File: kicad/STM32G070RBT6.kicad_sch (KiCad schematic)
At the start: 13 parts, among them J21 STM32-PROGRAM, J23 STM32-PROGRAM, U17 STM32G070RBT6, Y3 CRY-8MHz-3225-SMD

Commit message: Added Pi CM4/CM5
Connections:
- net CURENT-SENSE is gone; now on net PWR-BTN-SENSE: U17.17 (PA0)
- net VBAT-SENSE is gone; now on net PMIC_PWRON: U17.18 (PA1)
- net PMIC_PWRON: no longer U17.44 (PA12)
- net PWR-BTN-SENSE: no longer U17.43 (PA11)
- net CHARGE-STATUS renamed ~{CHG_INT}
- net MAIN-FAN-S-CTRL renamed SUCTION-FAN-FG
- net MAIN-FAN-S-SENSE renamed SUCTION-FAN-SP
- net RK-RESET renamed PI-RESET
- net V-CHARGE-SENSE renamed BAT_ID
- new net I2C2_SCL: U17.43 (PA11)
- new net I2C2_SDA: U17.44 (PA12)

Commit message: Changed MCU to STM32G473VCT6
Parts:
- removed C101: 100nF, oomwoo_altium:CAP-0402, symbol DesignLibrary:MCU-STM32_2_Capacitor-1_DesignLibrary.SchLib
- removed C102: 4.7uF, oomwoo_altium:CAP-0603, symbol DesignLibrary:MCU-STM32_2_Capacitor-1_DesignLibrary.SchLib
- removed C106, C107: 18pF, oomwoo_altium:CAP-0402, symbol DesignLibrary:MCU-STM32_2_Capacitor-1_DesignLibrary.SchLib
- removed C18: 100nF, oomwoo_altium:CAP-0402, symbol DesignLibrary:MCU-STM32_3_Capacitor-1_DesignLibrary.SchLib
- removed D15: SS34/NC, oomwoo_altium:SMA, symbol DesignLibrary:MCU-STM32_0_DIODE-2_DesignLibrary.SchLib
- removed J21: STM32-PROGRAM, oomwoo_altium:HDR1X5, symbol DesignLibrary:MCU-STM32_0_mirrored_HDRx5_DesignLibrary.SchLib
- removed R134: 10K, oomwoo_altium:RES-0402, symbol DesignLibrary:MCU-STM32_3_Resistor-1_DesignLibrary.SchLib
- removed R135: 0.01R, oomwoo_altium:RES-0805-S, symbol DesignLibrary:MCU-STM32_2_Resistor-1_DesignLibrary.SchLib
- removed R86: 0R, oomwoo_altium:RES-0402, symbol DesignLibrary:MCU-STM32_0_Resistor-1_DesignLibrary.SchLib
- removed U17: STM32G070RBT6, oomwoo_altium:QFP50P1200X1200X160-64N, symbol DesignLibrary:MCU-STM32_0_STM32G070RBT6_DesignLibrary.SchLib
- removed Y3: CRY-8MHz-3225-SMD, oomwoo_altium:X4B250_320H120_SMD, symbol DesignLibrary:MCU-STM32_0_CRY-24MHz-3225-SMD_0_DesignLibrary.SchLib
- added C12, C13, C14, C15, C16, C30, C32, C37: 100nF/10V, Capacitor_SMD:C_0603_1608Metric, symbol Device:C_Small
- added C17, C31, C33: 4.7uF/10V, Capacitor_SMD:C_0603_1608Metric, symbol Device:C_Small
- added C34, C35: 22pF/10V, Capacitor_SMD:C_0603_1608Metric, symbol Device:C_Small
- added D3, D5: SS34, Diode_SMD:D_SMA, symbol Diode:SS34
- added J21: STM-PROGRAM, Connector_PinHeader_2.54mm:PinHeader_1x05_P2.54mm_Vertical, symbol Connector:Conn_01x05_Pin
- added JTAG1: STLINK-V3MINIE, JLCImport:FTSH-107-01-L-DV-K-A, symbol JLCImport:FTSH-107-01-L-DV-K-A
- added R16: 0.01, Resistor_SMD:R_0603_1608Metric, symbol Device:R_US
- added R19: 0, Resistor_SMD:R_0603_1608Metric, symbol Device:R_US
- added R21, R22: 10k, Resistor_SMD:R_0603_1608Metric, symbol Device:R_US
- added R33: 10, Resistor_SMD:R_0603_1608Metric, symbol Device:R_US
- added U13: STM32G473VCT6, footprints:LQFP100-14x14mm, symbol 2026-07-20_14-00-45:STM32G473VCT6
- added X1: ABM3-8_000MHZ-D2Y-T, JLCImport:ABM3-8_000MHZ-D2Y-T, symbol JLCImport:ABM3-8_000MHZ-D2Y-T
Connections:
- net ANTI-FALL-LEFT-DOWN-ADC: now also U13.21 (PA1)
- net ANTI-FALL-LEFT-UP-ADC: now also U13.20 (PA0)
- net ANTI-FALL-RIGHT-DOWN-ADC: now also U13.25 (PA3)
- net ANTI-FALL-RIGHT-UP-ADC: now also U13.22 (PA2)
- net BAT_ID: now also U13.53 (PB14)
- net GND: now also C12.2, C13.2, C14.2, C15.2, C16.2, C17.2, C30.2, C31.2, C32.2, C33.2, C34.2, C35.2, C37.2, J21.4 (Pin_4), JTAG1.05 (5), JTAG1.07 (7), R22.1, U13.23 (VSS), U13.35 (VSSA), U13.48 (VSS), U13.63 (VSS), U13.74 (VSS), U13.99 (VSS)
- net HOME-BTN: now also U13.79 (PC10)
- net IMU-FSYNC: now also U13.86 (PD4)
- net IMU-INT#1: now also U13.85 (PD3)
- net IMU-INT#2: now also U13.84 (PD2)
- net IMU-SPI-CS: now also U13.93 (PB6)
- net IMU-SPI-MISO: now also U13.91 (PB4)
- net IMU-SPI-MOSI: now also U13.92 (PB5)
- net IMU-SPI-SCLK: now also R33.2
- net LED-HOME: now also U13.80 (PC11)
- net LED-PWR: now also U13.28 (PA6)
- net LiDAR-M-CTRL: now also U13.17 (PC2)
- net MAIN-FAN-V-CTRL: now also U13.82 (PD0)
- net PC14: now also U13.8 (PC14-OSC32_IN)
- net PC15: now also U13.9 (PC15-OSC32_OUT)
- net PI-RESET: now also U13.52 (PB13)
- net PMIC_PWRON: now also U13.73 (PA12)
- net PWR-BTN-SENSE: now also U13.72 (PA11)
- net SIDE-PROXI-LEFT: now also U13.87 (PD5)
- net SIDE-PROXI-RIGHT: now also U13.55 (PD8)
- net STM-PWR-CTRL: now also U13.78 (PA15)
- net STM-RESET: now also C37.1, J21.3 (Pin_3), JTAG1.12, R21.1, U13.14 (PG10-NRST)
- net STM32-SWCLK: now also J21.2 (Pin_2), JTAG1.06 (6), U13.77 (PA14)
- net STM32-SWDIO: now also J21.1 (Pin_1), JTAG1.04 (4), U13.76 (PA13)
- net STM32-UART1-RX: now also JTAG1.13, U13.31 (PC5)
- net STM32-UART1-TX: now also JTAG1.14, U13.30 (PC4)
- net TOUCHL: now also U13.88 (PD6)
- net TOUCHR: now also U13.56 (PD9)
- net VCC-3V3-P: now also C12.1, C13.1, C14.1, C15.1, C16.1, C17.1, C30.1, C31.1, C32.1, C33.1, D3.1 (K), D5.1 (K), R16.1, R21.2, U13.100 (VDD), U13.24 (VDD), U13.36 (VREF+), U13.37 (VDDA), U13.49 (VDD), U13.64 (VDD), U13.75 (VDD)
- net WATER-PUMP-SENSE-ADC: now also U13.27 (PA5)
- net WATER-PUMPU-CTRL: now also U13.15 (PC0)
- net WHEEL-M-L-F-ADC: now also U13.58 (PD11)
- net WHEEL-M-LEFT-ENCODE-A: now also U13.70 (PA9)
- net WHEEL-M-LEFT-IN1: now also U13.69 (PA8)
- net WHEEL-M-LEFT-IN2: now also U13.29 (PA7)
- net WHEEL-M-R-F-ADC: now also U13.57 (PD10)
- net WHEEL-M-RIGHT-ENCODE-A: now also U13.71 (PA10)
- net WHEEL-M-RIGHT-IN1: now also U13.94 (PB7)
- net WHEEL-M-RIGHT-IN2: now also U13.96 (PB9)
- net ~{CHG_INT}: now also U13.54 (PB15)
- new net: R19.1, U13.13 (PF1-OSC_OUT)
- new net: C35.1, R19.2, X1.2 (OSC2)
- new net: R33.1, U13.90 (PB3)
- new net: R22.2, U13.95 (PB8-BOOT0)
- new net: D5.2 (A), JTAG1.03 (3)
- new net: C34.1, U13.12 (PF0-OSC_IN), X1.1 (OSC1)
- new net: R16.2, U13.6 (VBAT)
- new net: D3.2 (A), J21.5 (Pin_5)
- new net I2C3_SCL: U13.67 (PC8)
- new net I2C3_SDA: U13.68 (PC9)
- new net MAIN-BRUSH-CURRENT-ADC: U13.26 (PA4)
- new net MAIN-BRUSH-IN1: U13.61 (PD14)
- new net MAIN-BRUSH-IN2: U13.62 (PD15)
- new net MAIN-FAN-S-CTRL: U13.83 (PD1)
- new net MAIN-FAN-S-SENSE: U13.81 (PC12)
- new net SIDE-BRUSH-CURRENT-ADC: U13.60 (PD13)
- new net SIDE-BRUSH-IN1: U13.65 (PC6)
- new net SIDE-BRUSH-IN2: U13.66 (PC7)
- no-connect marks 0 -> 36
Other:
- note added: "MCU STM32G473"
- note removed: "MCU STM32G070"
- moved on the sheet: J23

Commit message: STM32G473VCT6
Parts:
- removed D3: SS34, Diode_SMD:D_SMA, symbol Diode:SS34
- removed J21: STM-PROGRAM, Connector_PinHeader_2.54mm:PinHeader_1x05_P2.54mm_Vertical, symbol Connector:Conn_01x05_Pin
- removed J23: STM32-PROGRAM, oomwoo_altium:HDR1X5, symbol DesignLibrary:MCU-STM32_0_mirrored_HDRx5_DesignLibrary.SchLib
- removed R33: 10, Resistor_SMD:R_0603_1608Metric, symbol Device:R_US
- added MCU_IO1: Conn_02x24_Odd_Even, symbol Connector_Generic:Conn_02x24_Odd_Even
- added R64: 10, symbol Device:R_US
- added STM_DEBUG1: Conn_01x05_Pin, symbol Connector:Conn_01x05_Pin
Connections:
- net GND: now also MCU_IO1.10 (Pin_10), MCU_IO1.12 (Pin_12), MCU_IO1.14 (Pin_14), MCU_IO1.16 (Pin_16), MCU_IO1.18 (Pin_18), MCU_IO1.2 (Pin_2), MCU_IO1.20 (Pin_20), MCU_IO1.22 (Pin_22), MCU_IO1.24 (Pin_24), MCU_IO1.26 (Pin_26), MCU_IO1.28 (Pin_28), MCU_IO1.30 (Pin_30), MCU_IO1.32 (Pin_32), MCU_IO1.34 (Pin_34), MCU_IO1.36 (Pin_36), MCU_IO1.38 (Pin_38), MCU_IO1.4 (Pin_4), MCU_IO1.40 (Pin_40), MCU_IO1.42 (Pin_42), MCU_IO1.44 (Pin_44), MCU_IO1.46 (Pin_46), MCU_IO1.48 (Pin_48), MCU_IO1.6 (Pin_6), MCU_IO1.8 (Pin_8), STM_DEBUG1.1 (Pin_1)
- net HOME-BTN: now also U13.34 (PB2); no longer U13.79 (PC10)
- net IMU-SPI-SCLK: now also R64.1
- net LED-HOME: now also U13.51 (PB12); no longer U13.80 (PC11)
- net PC14: now also MCU_IO1.7 (Pin_7)
- net PC15: now also MCU_IO1.9 (Pin_9)
- net SIDE-PROXI-LEFT: now also U13.89 (PD7); no longer U13.87 (PD5)
- net STM32-UART1-RX: now also STM_DEBUG1.4 (Pin_4)
- net STM32-UART1-TX: now also STM_DEBUG1.5 (Pin_5)
- net TOUCHL: now also U13.59 (PD12); no longer U13.88 (PD6)
- net VCC-3V3-P: now also MCU_IO1.3 (Pin_3)
- net at U13.90 (PB3): now also R64.2
- net CLIFF_LED_EN: now reaches U13.16 (PC1)
- net BUMPER_LED_EN: now reaches U13.18 (PC3)
- net WHEEL-M-RIGHT-DROP: now reaches U13.32 (PB0)
- net WHEEL-M-LEFT-DROP: now reaches U13.33 (PB1)
- net STM_UART3_TX: now reaches U13.47 (PB10)
- net STM_UART3_RX: now reaches U13.50 (PB11)
- net PC13: now reaches U13.7 (PC13)
- net PC13: now also MCU_IO1.5 (Pin_5)
- net PE2: now reaches U13.1 (PE2)
- net PE2: now also MCU_IO1.15 (Pin_15)
- net PF9: now reaches U13.10 (PF9)
- net PF9: now also MCU_IO1.45 (Pin_45)
- net PF10: now reaches U13.11 (PF10)
- net PF10: now also MCU_IO1.47 (Pin_47)
- net PF2: now reaches U13.19 (PF2)
- net PF2: now also MCU_IO1.43 (Pin_43)
- net PE3: now reaches U13.2 (PE3)
- net PE3: now also MCU_IO1.17 (Pin_17)
- net PE4: now reaches U13.3 (PE4)
- net PE4: now also MCU_IO1.19 (Pin_19)
- net PE7: now reaches U13.38 (PE7)
- net PE7: now also MCU_IO1.25 (Pin_25)
- net PE8: now reaches U13.39 (PE8)
- net PE8: now also MCU_IO1.27 (Pin_27)
- net PE5: now reaches U13.4 (PE5)
- net PE5: now also MCU_IO1.21 (Pin_21)
- net PE9: now reaches U13.40 (PE9)
- net PE9: now also MCU_IO1.29 (Pin_29)
- net PE10: now reaches U13.41 (PE10)
- net PE10: now also MCU_IO1.31 (Pin_31)
- net PE11: now reaches U13.42 (PE11)
- net PE11: now also MCU_IO1.33 (Pin_33)
- net PE12: now reaches U13.43 (PE12)
- net PE12: now also MCU_IO1.35 (Pin_35)
- net PE13: now reaches U13.44 (PE13)
- net PE13: now also MCU_IO1.37 (Pin_37)
- net PE14: now reaches U13.45 (PE14)
- net PE14: now also MCU_IO1.39 (Pin_39)
- net PE15: now reaches U13.46 (PE15)
- net PE15: now also MCU_IO1.41 (Pin_41)
- net PE6: now reaches U13.5 (PE6)
- net PE6: now also MCU_IO1.23 (Pin_23)
- net PE0: now reaches U13.97 (PE0)
- net PE0: now also MCU_IO1.11 (Pin_11)
- net PE1: now reaches U13.98 (PE1)
- net PE1: now also MCU_IO1.13 (Pin_13)
- net STM-RESET renamed STM32-RST
- new net USART4-IR-L-RX: U13.88 (PD6)
- new net USART4-IR-L-TX: U13.87 (PD5)
- new net USART4-IR-R-RX: U13.80 (PC11)
- new net USART4-IR-R-TX: U13.79 (PC10)
- new net VCC-5V-REG: MCU_IO1.1 (Pin_1)
- no-connect marks 36 -> 8
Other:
- note added: "Compatible with TTL-234X-3V3 smart cable"
- moved on the sheet: C12, C13, C14, C15, C16, C17, C30, C31, C32, C33, C34, C35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

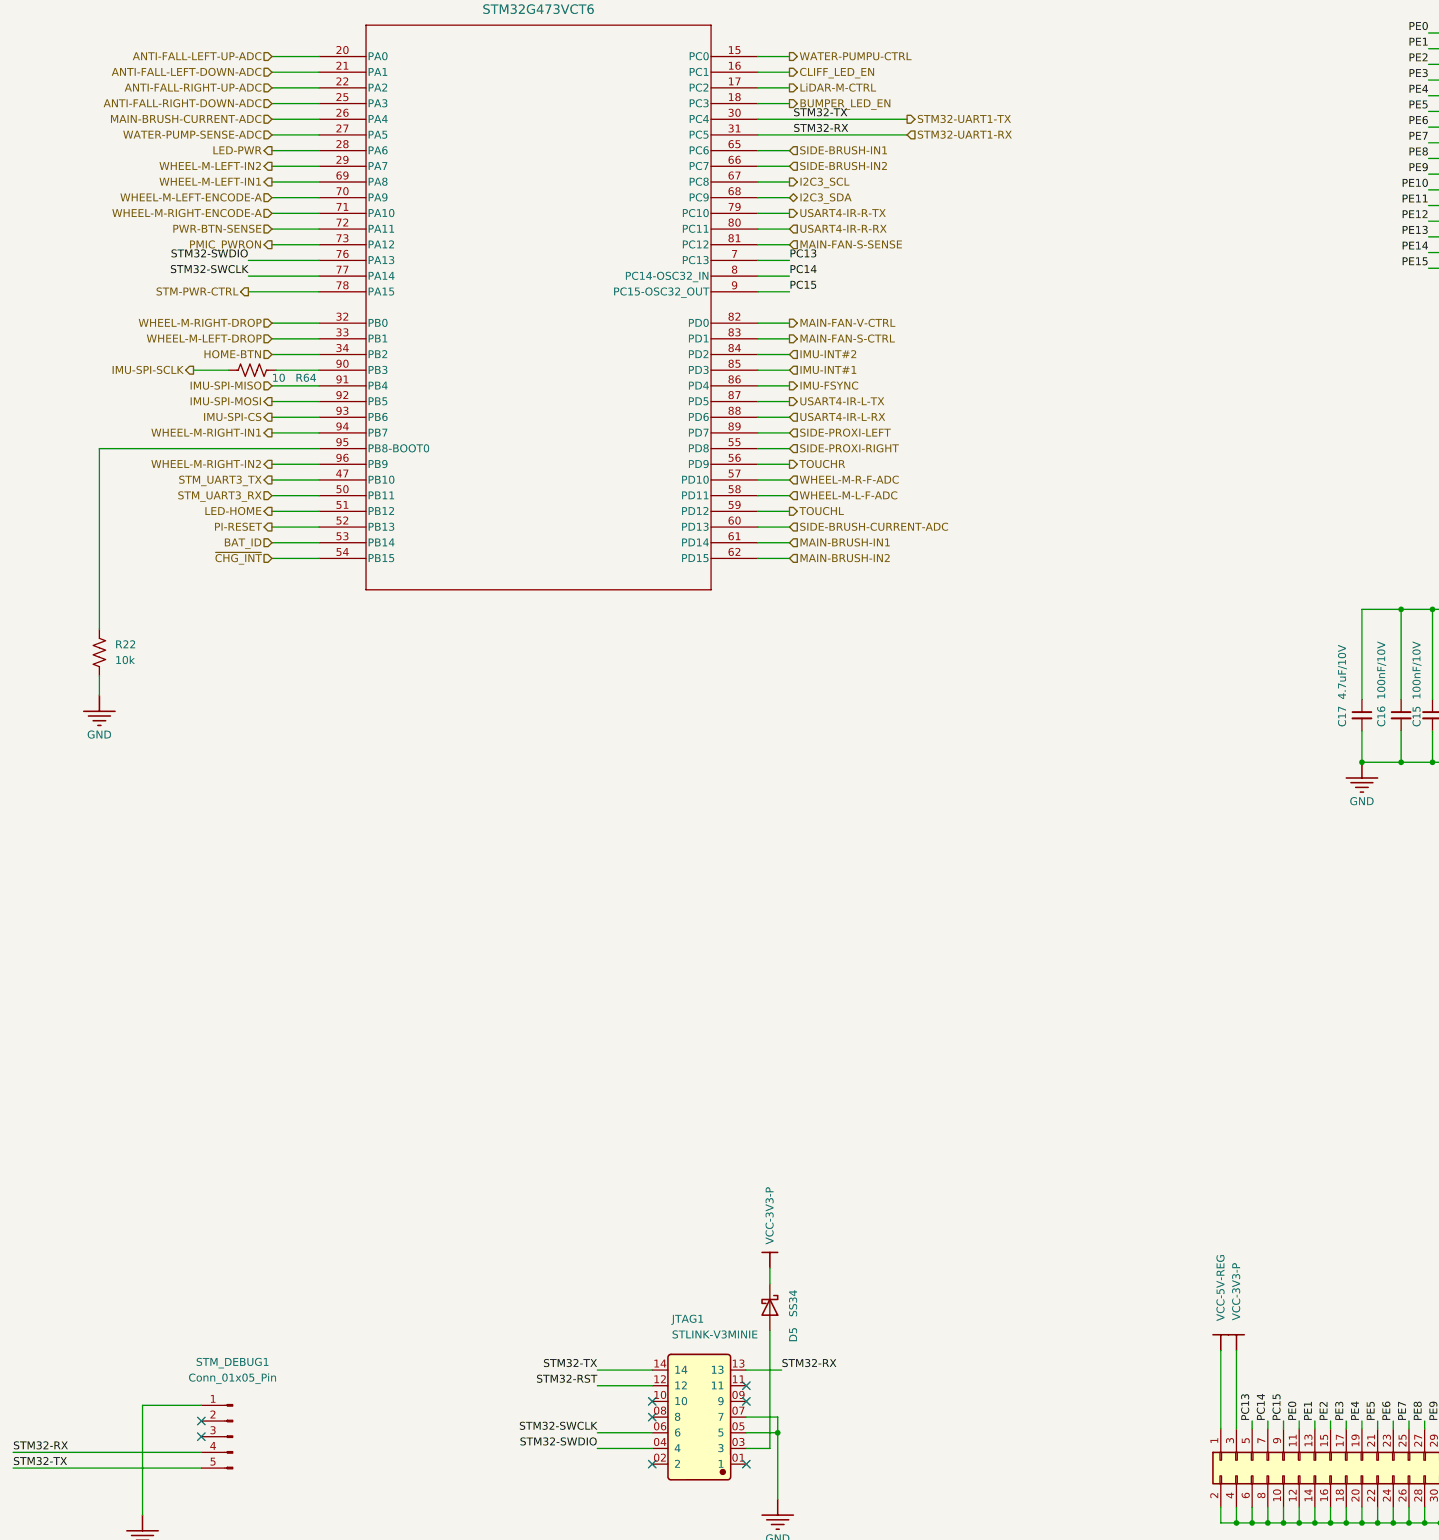
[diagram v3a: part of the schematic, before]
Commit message: RTC clock, signal integrity
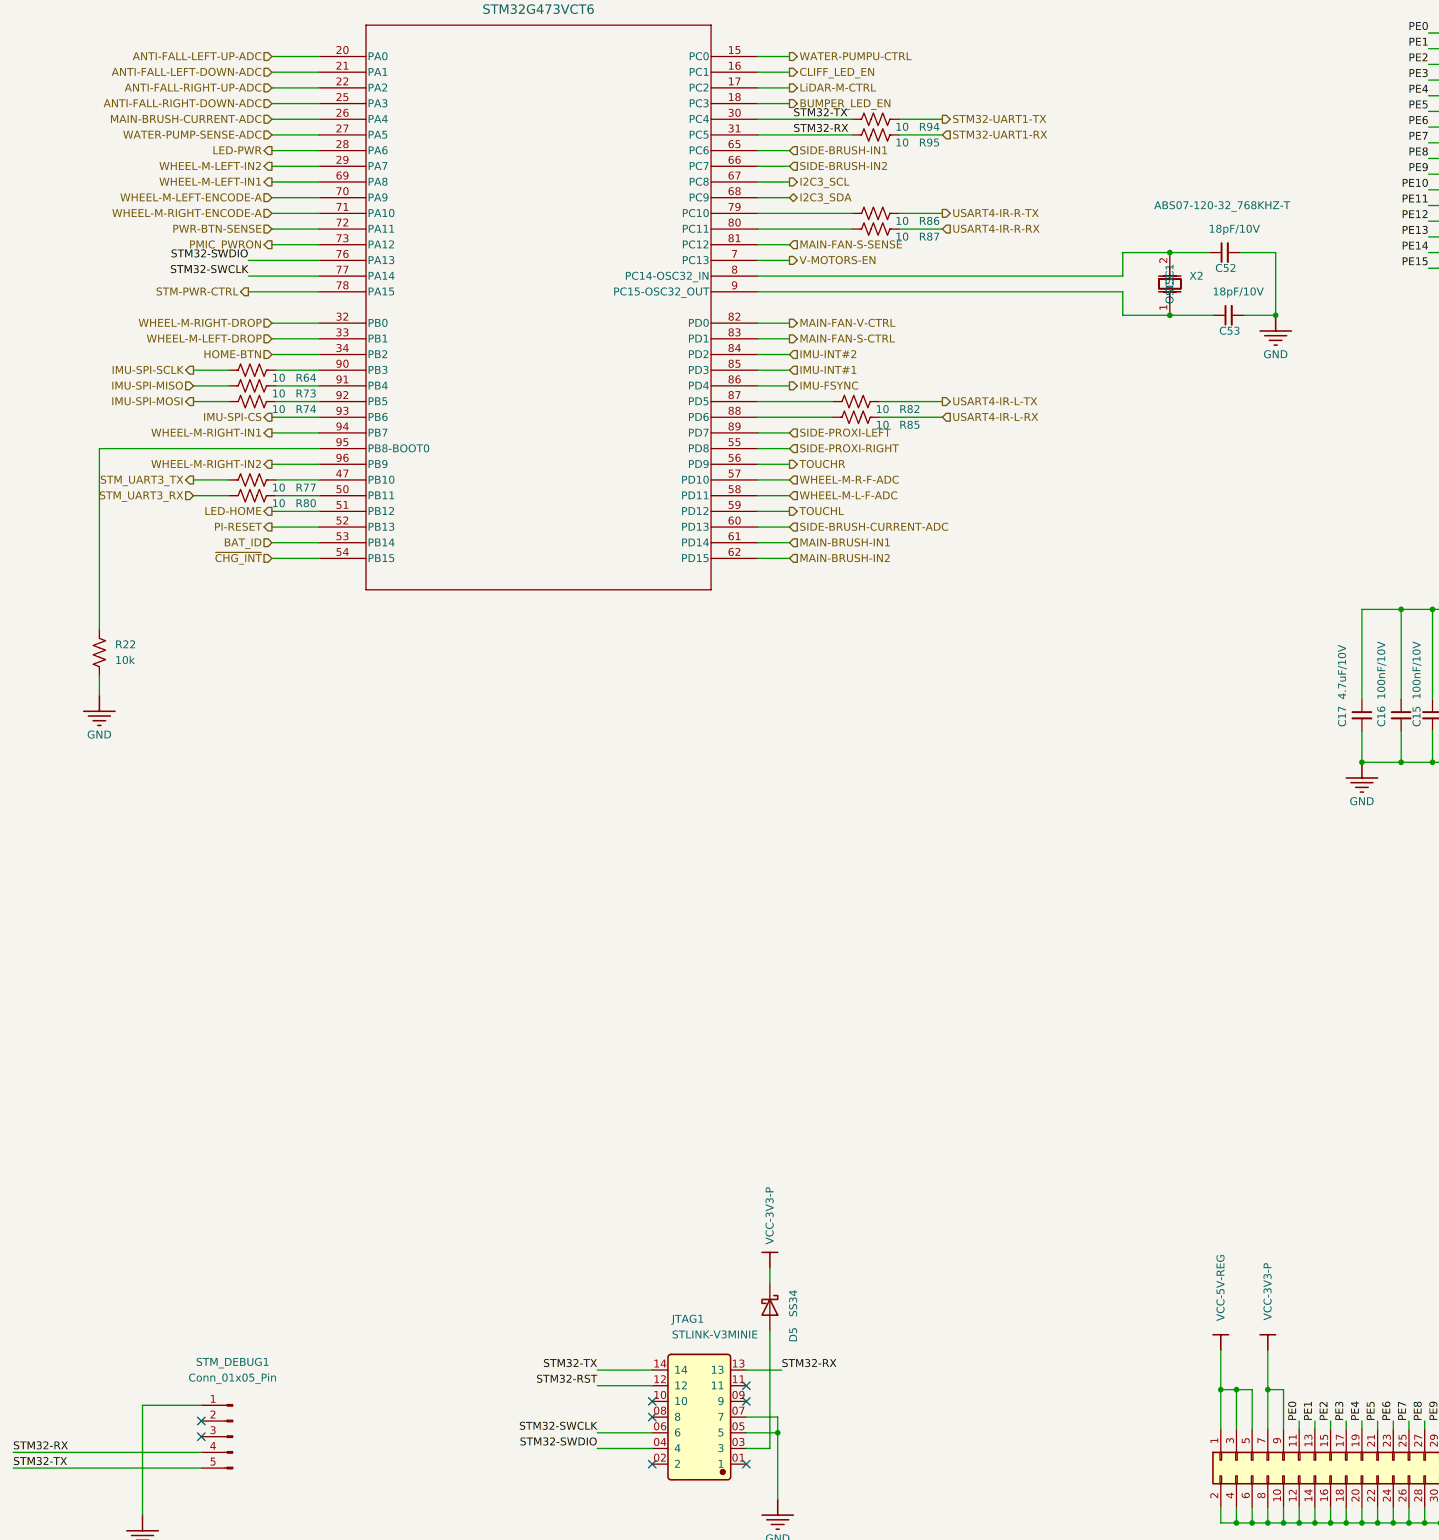
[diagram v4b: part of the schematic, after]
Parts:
- added C52, C53: 18pF/10V, Capacitor_SMD:C_0603_1608Metric, symbol Device:C_Small
- added R73, R74, R77, R80, R82, R85, R86, R87, R94, R95: 10, symbol Device:R_US
- added X2: ABS07-120-32_768KHZ-T, JLCImport:ABS07-120-32_768KHZ-T, symbol JLCImport:ABS07-120-32_768KHZ-T
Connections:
- net GND: now also C52.2, C53.2
- net IMU-SPI-MISO: now also R73.1; no longer U13.91 (PB4)
- net IMU-SPI-MOSI: now also R74.1; no longer U13.92 (PB5)
- net STM32-UART1-RX: now also R95.2; no longer JTAG1.13, STM_DEBUG1.4 (Pin_4), U13.31 (PC5)
- net STM32-UART1-TX: now also R94.2; no longer JTAG1.14, STM_DEBUG1.5 (Pin_5), U13.30 (PC4)
- net STM_UART3_RX: now also R80.1; no longer U13.50 (PB11)
- net STM_UART3_TX: now also R77.1; no longer U13.47 (PB10)
- net USART4-IR-L-RX: now also R85.2; no longer U13.88 (PD6)
- net USART4-IR-L-TX: now also R82.2; no longer U13.87 (PD5)
- net USART4-IR-R-RX: now also R87.2; no longer U13.80 (PC11)
- net USART4-IR-R-TX: now also R86.2; no longer U13.79 (PC10)
- net VCC-3V3-P: now also MCU_IO1.7 (Pin_7), MCU_IO1.9 (Pin_9); no longer MCU_IO1.3 (Pin_3)
- net VCC-5V-REG: now also MCU_IO1.3 (Pin_3), MCU_IO1.5 (Pin_5)
- net PC13 renamed V-MOTORS-EN
- net V-MOTORS-EN: no longer MCU_IO1.5 (Pin_5)
- net PC14: no longer names the net of U13.8 (PC14-OSC32_IN)
- net PC14: now also C52.1, X2.2 (OSC2); no longer MCU_IO1.7 (Pin_7)
- net PC15: no longer names the net of U13.9 (PC15-OSC32_OUT)
- net PC15: now also C53.1, X2.1 (OSC1); no longer MCU_IO1.9 (Pin_9)
- new net: R82.1, U13.87 (PD5)
- new net: R77.2, U13.47 (PB10)
- new net: R80.2, U13.50 (PB11)
- new net: R86.1, U13.79 (PC10)
- new net: R87.1, U13.80 (PC11)
- new net: R85.1, U13.88 (PD6)
- new net: R73.2, U13.91 (PB4)
- new net: R74.2, U13.92 (PB5)
- new net STM32-RX: JTAG1.13, R95.1, STM_DEBUG1.4 (Pin_4), U13.31 (PC5)
- new net STM32-TX: JTAG1.14, R94.1, STM_DEBUG1.5 (Pin_5), U13.30 (PC4)

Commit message: External RTC; IR light; side sensors
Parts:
- removed C52, C53: 18pF/10V, Capacitor_SMD:C_0603_1608Metric, symbol Device:C_Small
- removed R77: 10, symbol Device:R_US
- removed X2: ABS07-120-32_768KHZ-T, JLCImport:ABS07-120-32_768KHZ-T, symbol JLCImport:ABS07-120-32_768KHZ-T
- added R113, R117: 10, symbol Device:R_US
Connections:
- net SIDE-PROXI-LEFT is gone; now on net IMU-INT#2: U13.89 (PD7)
- net IMU-INT#2: no longer U13.84 (PD2)
- net MAIN-FAN-S-SENSE: now also U13.40 (PE9); no longer U13.81 (PC12)
- net PE0: now also MCU_IO1.13 (Pin_13); no longer MCU_IO1.11 (Pin_11)
- net PE1: now also MCU_IO1.15 (Pin_15); no longer MCU_IO1.13 (Pin_13)
- net PE15: no longer U13.46 (PE15)
- net PE2: now also MCU_IO1.17 (Pin_17); no longer MCU_IO1.15 (Pin_15)
- net PE3: now also MCU_IO1.19 (Pin_19); no longer MCU_IO1.17 (Pin_17)
- net PE4: now also MCU_IO1.21 (Pin_21); no longer MCU_IO1.19 (Pin_19)
- net PE5: now also MCU_IO1.23 (Pin_23); no longer MCU_IO1.21 (Pin_21)
- net PE6: now also MCU_IO1.25 (Pin_25); no longer MCU_IO1.23 (Pin_23)
- net PE7: now also MCU_IO1.27 (Pin_27); no longer MCU_IO1.25 (Pin_25)
- net PE8: now also MCU_IO1.29 (Pin_29); no longer MCU_IO1.27 (Pin_27)
- net VCC-3V3-P: now also MCU_IO1.3 (Pin_3); no longer MCU_IO1.7 (Pin_7), MCU_IO1.9 (Pin_9)
- net VCC-5V-REG: no longer MCU_IO1.3 (Pin_3), MCU_IO1.5 (Pin_5)
- net PC14: now reaches U13.8 (PC14-OSC32_IN)
- net PC14: now also MCU_IO1.5 (Pin_5)
- net PC15: now reaches U13.9 (PC15-OSC32_OUT)
- net PC15: now also MCU_IO1.7 (Pin_7)
- removed net PE9: MCU_IO1.29 (Pin_29), U13.40 (PE9)
- net SIDE-PROXI-RIGHT renamed PD8
- net PD8: now also MCU_IO1.9 (Pin_9)
- net STM_UART3_RX renamed UART3_RX2
- net TOUCHL renamed LIGHT-ON
- net TOUCHR renamed PD9
- net PD9: now also MCU_IO1.11 (Pin_11)
- net USART4-IR-L-RX renamed USART2-IR-L-RX
- net USART4-IR-L-TX renamed USART2-IR-L-TX
- net V-MOTORS-EN: no longer names the net of U13.7 (PC13)
- new net: R113.1, U13.84 (PD2)
- new net: R117.1, U13.81 (PC12)
- new net UART3_RX1: U13.46 (PE15)
- new net UART5_RX: R113.2
- new net UART5_TX: R117.2
- no-connect marks 8 -> 10
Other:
- moved on the sheet: MCU_IO1
